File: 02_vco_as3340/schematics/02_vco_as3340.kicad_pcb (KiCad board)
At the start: 2 copper layers, 75 x 100 mm, 91 parts, among them J10 Outputs, J11 SQUARE OUT, J12 TRI OUT, J13 SAW OUT, J14 SINE OUT, J5 Tuning, J6 Sync Mode, J7 FM & PWM, J8 Mode Switch, J9 Panel Power, Q1 BC547C, Q2 BC547C, U1 TL072, U2 AS3340, U3 TL074

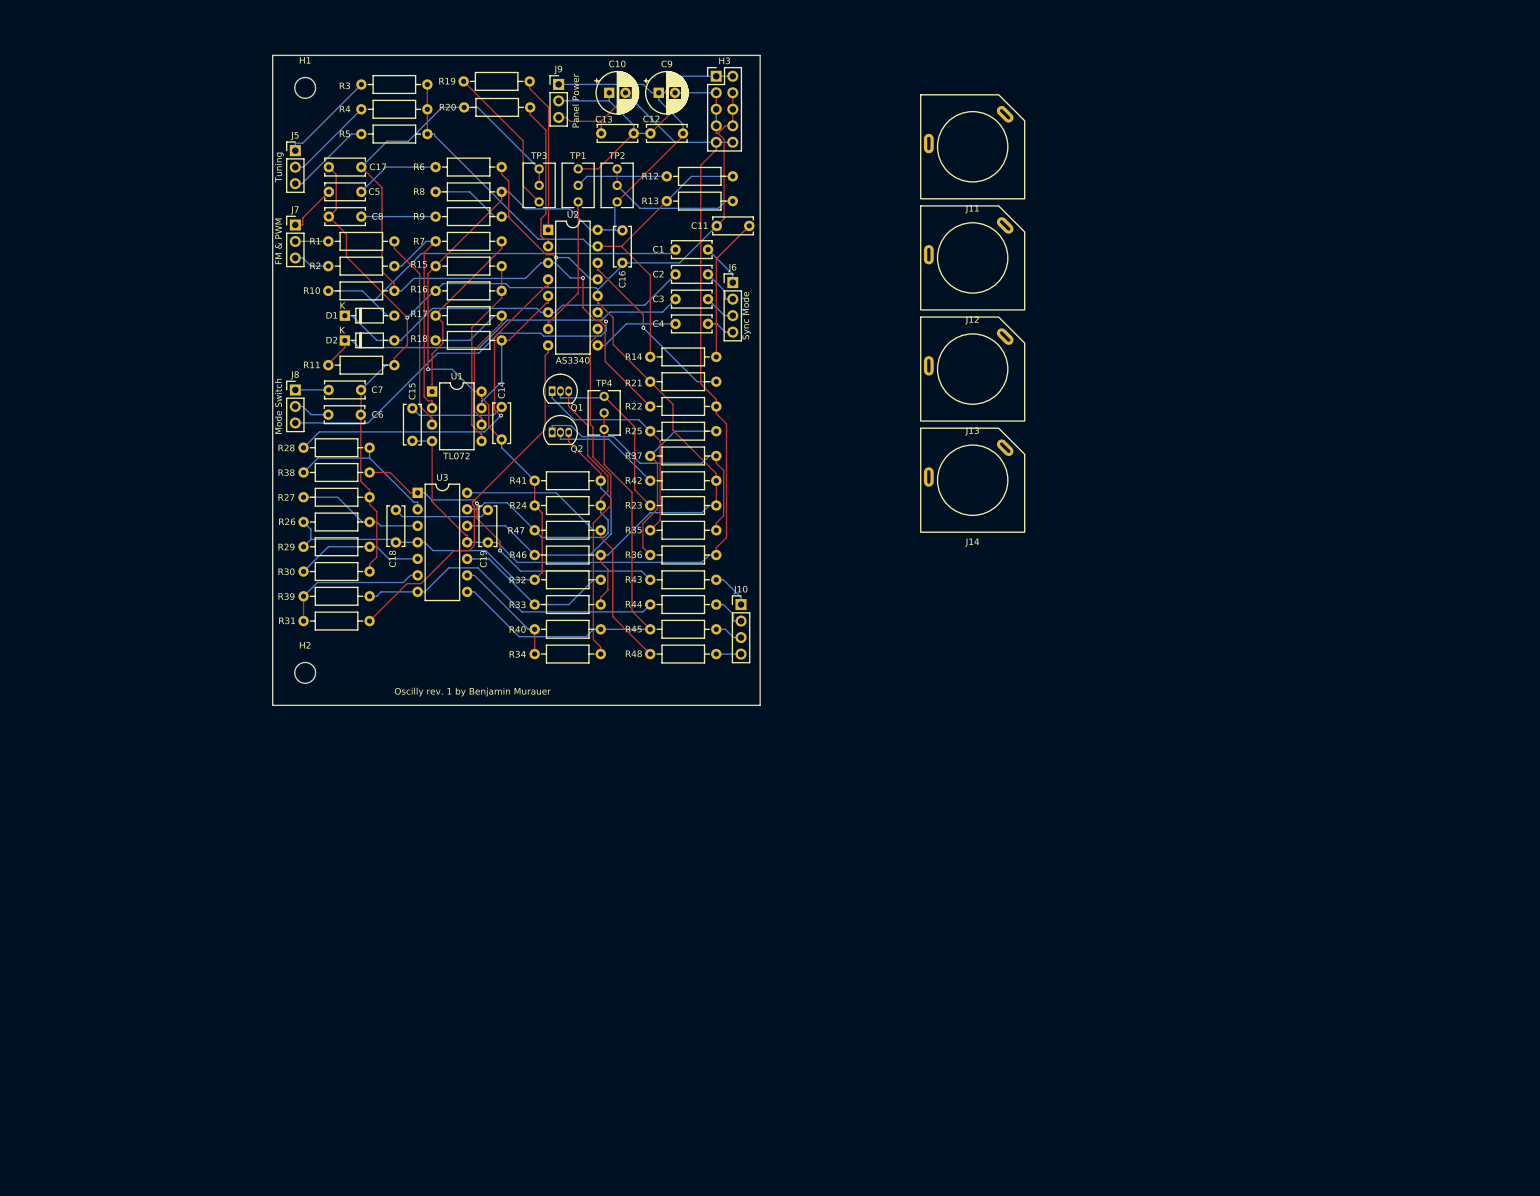
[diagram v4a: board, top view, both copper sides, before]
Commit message: made sub board for 02
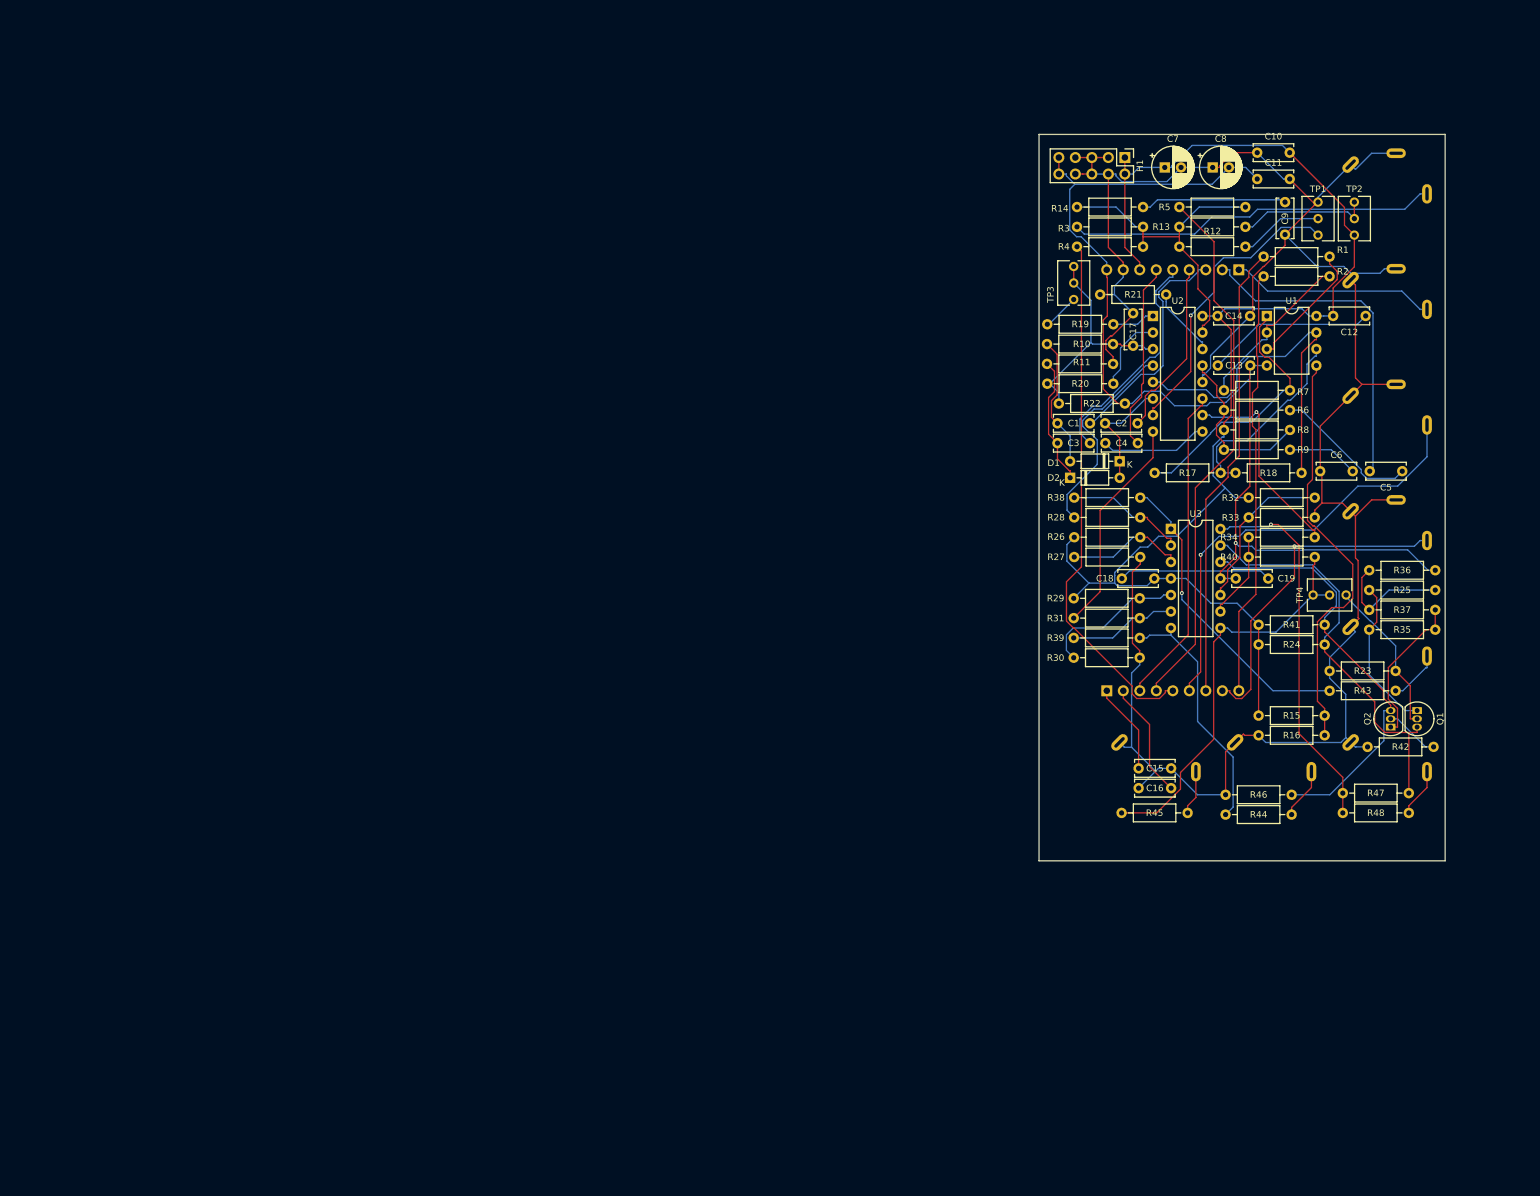
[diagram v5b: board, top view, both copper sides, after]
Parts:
- removed H2: MountingHole, MountingHole:MountingHole_3.2mm_M3
- removed H3: Eurorack 10 pin header, Connector_PinHeader_2.54mm:PinHeader_2x05_P2.54mm_Vertical
- removed J11: SQUARE OUT, cynthia:6.35 mm jack socket mono
- removed J12: TRI OUT, cynthia:6.35 mm jack socket mono
- removed J13: SAW OUT, cynthia:6.35 mm jack socket mono
- removed J14: SINE OUT, cynthia:6.35 mm jack socket mono
- added J1: Header 1, Connector_PinHeader_2.54mm:PinHeader_1x09_P2.54mm_Vertical, B.Cu at (175.6, 59.0)
- added J2: Header 2, Connector_PinHeader_2.54mm:PinHeader_1x09_P2.54mm_Vertical, B.Cu at (155.3, 123.8)
- added J3: SYNC IN, cynthia:6.35 mm jack socket mono switched, B.Cu at (197.8, 83.4)
- added J4: FM IN, cynthia:6.35 mm jack socket mono switched, B.Cu at (197.8, 65.6)
- C10: value 47uF -> 100nF; footprint Capacitor_THT:CP_Radial_D6.3mm_P2.50mm -> Capacitor_THT:C_Disc_D6.0mm_W2.5mm_P5.00mm
- C11: value 10nF -> 100nF
- C15: value 100nF -> 10nF
- C16: value 100nF -> 820pF
- C7: value 820pF -> 47uF; footprint Capacitor_THT:C_Disc_D6.0mm_W2.5mm_P5.00mm -> Capacitor_THT:CP_Radial_D6.3mm_P2.50mm
- C8: value 10nF -> 47uF; footprint Capacitor_THT:C_Disc_D6.0mm_W2.5mm_P5.00mm -> Capacitor_THT:CP_Radial_D6.3mm_P2.50mm
- C9: value 47uF -> 10nF; footprint Capacitor_THT:CP_Radial_D6.3mm_P2.50mm -> Capacitor_THT:C_Disc_D6.0mm_W2.5mm_P5.00mm
- H1: value MountingHole -> Eurorack 10 pin header; footprint MountingHole:MountingHole_3.2mm_M3 -> Connector_PinHeader_2.54mm:PinHeader_2x05_P2.54mm_Vertical
- J10: value Outputs -> SINE OUT; footprint Connector_PinHeader_2.54mm:PinHeader_1x04_P2.54mm_Vertical -> cynthia:6.35 mm jack socket mono; moved to B.Cu
- J5: value Tuning -> PWM CV IN; footprint Connector_PinHeader_2.54mm:PinHeader_1x03_P2.54mm_Vertical -> cynthia:6.35 mm jack socket mono switched; moved to B.Cu
- J6: value Sync Mode -> 1V per O IN; footprint Connector_PinHeader_2.54mm:PinHeader_1x04_P2.54mm_Vertical -> cynthia:6.35 mm jack socket mono switched; moved to B.Cu
- J7: value FM & PWM -> SQUARE OUT; footprint Connector_PinHeader_2.54mm:PinHeader_1x03_P2.54mm_Vertical -> cynthia:6.35 mm jack socket mono; moved to B.Cu
- J8: value Mode Switch -> SAW OUT; footprint Connector_PinHeader_2.54mm:PinHeader_1x03_P2.54mm_Vertical -> cynthia:6.35 mm jack socket mono; moved to B.Cu
- J9: value Panel Power -> TRI OUT; footprint Connector_PinHeader_2.54mm:PinHeader_1x03_P2.54mm_Vertical -> cynthia:6.35 mm jack socket mono; moved to B.Cu
- moved J7 180.2 mm to (197.8, 118.9), turned to 180 degrees
- moved J5 178.0 mm to (197.8, 101.1), turned to 180 degrees
- moved C5 165.8 mm to (200.8, 90.0)
- moved J8 160.9 mm to (180.1, 136.7), turned to 180 degrees
- moved C6 152.9 mm to (188.2, 90.0)
- moved R15 144.3 mm to (178.7, 127.6)
- moved R1 143.9 mm to (179.5, 57.0)
- moved R16 143.9 mm to (178.7, 130.6)
- moved R2 143.9 mm to (179.5, 60.0)
- moved Q1 141.9 mm to (203.1, 126.8), turned to -90 degrees
- moved R47 140.4 mm to (201.8, 139.5), turned to 180 degrees
- moved J9 140.1 mm to (162.3, 136.7), turned to 180 degrees
- moved Q2 136.7 mm to (199.0, 129.3), turned to 90 degrees
- moved R6 136.7 mm to (183.5, 80.6), turned to 180 degrees
- moved R8 136.5 mm to (183.5, 83.6), turned to 180 degrees
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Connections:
- C1 pad 2: /PCB/Positive Hard Sync -> Hard Sync +
- C10 pad 2: -12V -> +12V
- C11 pad 1: Net-(C11-Pad1) -> -12V
- C12 pad 1: GND -> Net-(C12-Pad1)
- C13 pad 2: GND -> Net-(C12-Pad1)
- C14 pad 1: Net-(C14-Pad1) -> GND
- C15 pad 1: -12V -> Mode LFO
- C15 pad 2: Net-(C14-Pad1) -> GND
- C16 pad 2: +12V -> Mode VCO
- C2 pad 2: /PCB/Hard Sync -> Hard Sync
- C3 pad 2: /PCB/Negative Hard Sync -> Hard Sync -
- C4 pad 2: /PCB/Soft Sync -> Soft Sync
- C5 pad 2: /PCB/FM -> FM CV Levelled
- C6 pad 1: /PCB/Mode LFO -> GND
- C6 pad 2: GND -> Net-(C6-Pad2)
- C7 pad 1: GND -> +12V
- C7 pad 2: /PCB/Mode VCO -> GND
- C8 pad 2: Net-(C8-Pad2) -> -12V
- C9 pad 1: +12V -> Net-(C9-Pad1)
- J10 pad 1: /PCB/Square -> Net-(J10-T)
- J10 pad 2: /PCB/Saw -> GND
- J5 pad 1: /PCB/1V/O -> PWM CV Hot
- J5 pad 2: /PCB/Coarse Tune -> GND
- J5 pad 3: /PCB/Fine Tune -> GND
- J6 pad 1: /PCB/Positive Hard Sync -> Net-(J6-T)
- J6 pad 2: /PCB/Hard Sync -> GND
- J6 pad 3: /PCB/Negative Hard Sync -> GND
- J7 pad 1: /PCB/FM -> Net-(J7-T)
- J7 pad 2: /PCB/PWM Offset -> GND
- J8 pad 1: /PCB/Mode VCO -> Net-(J8-T)
- J8 pad 2: /PCB/Mode LFO -> GND
- J9 pad 1: +12V -> Net-(J9-T)
- R1 pad 1: /PCB/PWM Offset -> PWM Offset
- R14 pad 2: Net-(C11-Pad1) -> Net-(C9-Pad1)
- R2 pad 1: /PCB/PWM CV -> PWM CV Levelled
- R3 pad 1: /PCB/1V/O -> Net-(J6-T)
- R4 pad 1: /PCB/Coarse Tune -> Coarse Tuning
- R43 pad 2: /Output Board/SQUARE -> Net-(J7-T)
- R44 pad 2: /Output Board/SAW -> Net-(J8-T)
- R45 pad 2: /Output Board/TRI -> Net-(J9-T)
- R48 pad 2: /Output Board/SINE -> Net-(J10-T)
- R5 pad 1: /PCB/Fine Tune -> Fine Tuning
- R9 pad 1: Net-(C8-Pad2) -> Net-(C6-Pad2)
- U2 pad 11: /PCB/Mode -> Mode COM
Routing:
- net Fine Tuning: track 0.00 -> 82.9 mm
- net Coarse Tuning: track 0.00 -> 81.5 mm
- net Net-(U2-VEE): track 115.0 -> 35.7 mm, vias 1 -> 0
- net GND: track 270.7 -> 341.6 mm, vias 1 -> 0
- net PWM Offset: track 0.00 -> 70.5 mm
- net Sync COM: track 0.00 -> 67.6 mm, vias 0 -> 1
- net PWM CV Levelled: track 0.00 -> 65.9 mm
- net /PCB/Mode: track 57.4 -> 0.00 mm, vias 1 -> 0
- net Net-(J6-T): track 0.00 -> 56.9 mm
- net PWM CV Hot: track 0.00 -> 51.2 mm, vias 0 -> 1
- net FM CV Levelled: track 0.00 -> 51.0 mm
- net Mode COM: track 0.00 -> 49.1 mm
- net Net-(D1-A): track 61.6 -> 20.2 mm
- net Net-(D2-K): track 59.3 -> 19.8 mm
- net Net-(D1-K): track 57.3 -> 18.3 mm
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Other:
- board size 75 x 100 mm -> 62.5 x 111.8 mm
- board text removed: "Oscilly rev. 1 by Benjamin Murauer"

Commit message: routed everyting
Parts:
- removed J1: Header 1, Connector_PinHeader_2.54mm:PinHeader_1x09_P2.54mm_Vertical
- removed J2: Header 2, Connector_PinHeader_2.54mm:PinHeader_1x09_P2.54mm_Vertical
- added J11: Header 1, Connector_PinSocket_2.54mm:PinSocket_2x05_P2.54mm_Vertical, F.Cu at (188.3, 109.3)
- added J12: Header 2, Connector_PinSocket_2.54mm:PinSocket_2x04_P2.54mm_Vertical, F.Cu at (160.8, 77.3)
- moved R14 75.2 mm to (216.9, 85.2), turned to 180 degrees
- moved R21 67.5 mm to (216.9, 88.2), turned to 180 degrees
- moved R4 60.6 mm to (206.7, 78.8)
- moved R3 59.4 mm to (206.7, 72.5)
- moved R46 58.5 mm to (216.9, 91.5)
- moved R13 58.5 mm to (216.9, 82.1), turned to 180 degrees
- moved C15 52.7 mm to (173.4, 84.7), turned to -90 degrees
- moved C16 51.8 mm to (177.0, 89.7), turned to 90 degrees
- moved R15 51.0 mm to (147.5, 87.2)
- moved TP1 50.2 mm to (163.3, 92.3)
- moved C3 49.9 mm to (197.2, 92.8), turned to 180 degrees
- moved R5 48.0 mm to (206.7, 75.5)
- moved C2 47.8 mm to (198.8, 101.9), turned to 180 degrees
- moved R47 47.4 mm to (216.9, 94.6)
- moved R16 45.5 mm to (157.7, 90.3), turned to 180 degrees
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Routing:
- net PWM CV Levelled: track 65.9 -> 6.39 mm
- net GND: track 341.6 -> 388.8 mm
- net Net-(J6-T): track 56.9 -> 15.7 mm
- net Sync COM: track 67.6 -> 27.0 mm, vias 1 -> 0
- net Fine Tuning: track 82.9 -> 44.1 mm
- net Net-(R40-Pad2): track 63.3 -> 96.3 mm
- net Net-(U1A--): track 25.9 -> 54.6 mm
- net Net-(U2-VTO): track 31.9 -> 58.6 mm, vias 1 -> 0
- net FM CV Levelled: track 51.0 -> 24.4 mm
- net Net-(U2-VHFT): track 45.8 -> 19.8 mm, vias 1 -> 0
- net Net-(D2-K): track 19.8 -> 45.4 mm
- net Net-(R38-Pad2): track 47.5 -> 69.5 mm, vias 1 -> 0
- net +12V: track 211.2 -> 231.0 mm, vias 0 -> 1
- net Net-(U2-VLFI): track 26.8 -> 45.7 mm
- net Net-(U3C--): track 13.4 -> 32.0 mm
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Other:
- board size 62.5 x 111.8 mm -> 75 x 100 mm

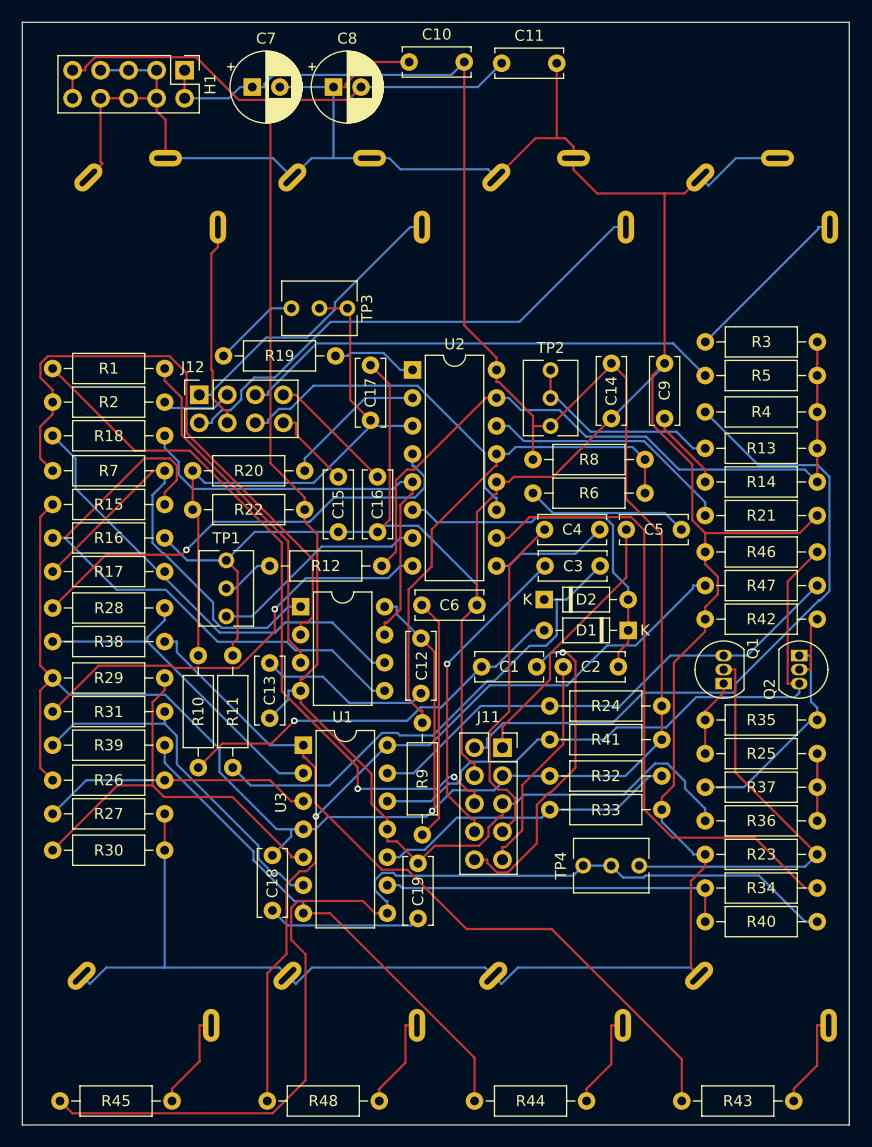
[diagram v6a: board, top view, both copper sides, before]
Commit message: fixed layout front/back
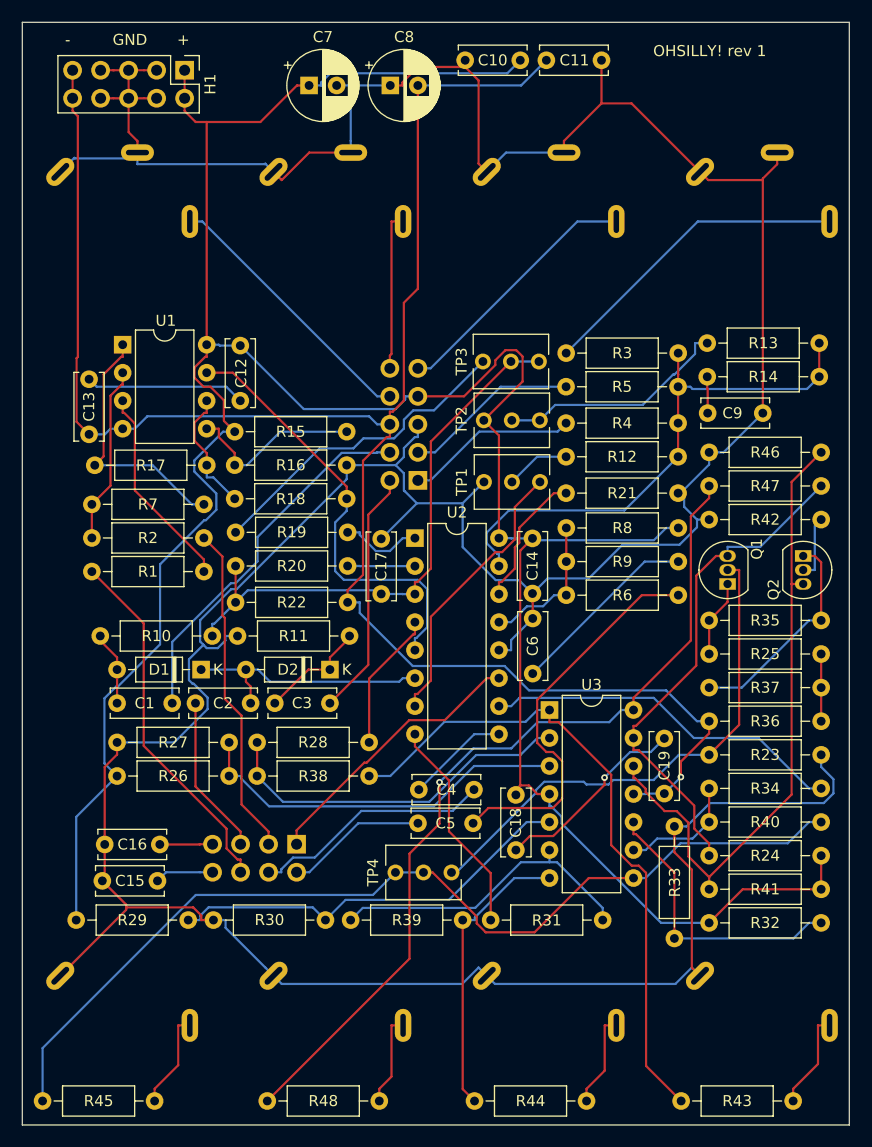
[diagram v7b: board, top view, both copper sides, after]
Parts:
- removed J11: Header 1, Connector_PinSocket_2.54mm:PinSocket_2x05_P2.54mm_Vertical
- removed J12: Header 2, Connector_PinSocket_2.54mm:PinSocket_2x04_P2.54mm_Vertical
- added J1: Header 1, Connector_PinSocket_2.54mm:PinSocket_2x05_P2.54mm_Vertical, B.Cu at (180.6, 85.0)
- added J2: Header 2, Connector_PinSocket_2.54mm:PinSocket_2x04_P2.54mm_Vertical, B.Cu at (169.6, 118.0)
- moved R31 44.0 mm to (187.2, 124.9)
- moved C15 40.1 mm to (157.0, 121.4), turned to 180 degrees
- moved D1 38.9 mm to (161.0, 102.2)
- moved C16 37.6 mm to (152.2, 118.0), turned to 0 degrees
- moved R9 34.0 mm to (204.3, 92.4), turned to 180 degrees
- moved C2 33.5 mm to (165.5, 105.2)
- moved C1 33.2 mm to (153.4, 105.2)
- moved C5 32.7 mm to (185.6, 116.1)
- moved C3 32.0 mm to (167.7, 105.2), turned to 0 degrees
- moved R39 31.3 mm to (174.5, 124.9)
- moved C12 31.2 mm to (164.5, 77.8)
- moved R28 31.2 mm to (176.2, 108.8), turned to 180 degrees
- moved C13 30.5 mm to (150.8, 80.9)
- moved C4 28.7 mm to (180.7, 113.1), turned to 0 degrees
- moved U1 28.7 mm to (153.9, 72.7)
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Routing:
- net Coarse Tuning: track 63.0 -> 15.6 mm
- net Net-(U1A--): track 54.6 -> 16.2 mm
- net Net-(U1B-+): track 54.4 -> 16.4 mm
- net Net-(D2-K): track 45.4 -> 10.0 mm
- net Net-(U2-VLFI): track 45.7 -> 13.2 mm
- net PWM Offset: track 65.2 -> 33.0 mm, vias 2 -> 0
- net Net-(U1B--): track 41.5 -> 11.3 mm
- net Net-(D1-A): track 36.5 -> 6.73 mm, vias 1 -> 0
- net Net-(U2-VP): track 41.9 -> 12.7 mm, vias 1 -> 0
- net Fine Tuning: track 44.1 -> 15.9 mm
- net Net-(U2-VTO): track 58.6 -> 32.9 mm
- net PWM CV Levelled: track 6.39 -> 30.2 mm
- net PWM CV Hot: track 46.7 -> 23.5 mm
- net Net-(R19-Pad1): track 7.95 -> 29.3 mm
- net Net-(C5-Pad1): track 14.8 -> 36.0 mm
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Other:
- board text added: "+"
- board text added: "-"
- board text added: "GND"
- board text added: "OHSILLY! rev 1"
